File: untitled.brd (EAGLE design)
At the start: 59.4 x 57.8 mm, 25 parts

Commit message: made the traces look better
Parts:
- moved C2 0.32 mm to (56.2, 34.0)
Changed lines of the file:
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@@
 <element name="U$2" library="SparkFun" package="LCC36" value="HMC6343A" x="86.995" y="23.495"/>
 <element name="C1" library="rcl" package="C0603" value="" x="48.26" y="41.275" rot="R180"/>
-<element name="C2" library="rcl" package="C0603" value="" x="56.515" y="33.9725" rot="R180"/>
+<element name="C2" library="rcl" package="C0603" value="" x="56.1975" y="33.9725" rot="R180"/>
 <element name="C3" library="rcl" package="C0603" value="" x="53.6575" y="51.1175" rot="R90"/>
 <element name="C4" library="SparkFun" package="0603" value="" x="79.6925" y="25.0825" rot="R90"/>
@@
 <wire x1="66.04" y1="36.83" x2="66.04" y2="24.765" width="0.3048" layer="1"/>
 <wire x1="66.04" y1="24.765" x2="68.58" y2="24.765" width="0.3048" layer="1"/>
-<wire x1="57.4" y1="38.5313" x2="58.1025" y2="36.83" width="0.254" layer="1"/>
+<wire x1="57.4" y1="38.5313" x2="57.4" y2="37.5325" width="0.3048" layer="1"/>
+<wire x1="57.4" y1="37.5325" x2="58.1025" y2="36.83" width="0.3048" layer="1"/>
 </signal>
 <signal name="N$6">
@@
 <wire x1="70.8025" y1="24.13" x2="70.485" y2="27.305" width="0.3048" layer="1"/>
 <wire x1="70.485" y1="27.305" x2="68.58" y2="27.305" width="0.3048" layer="1"/>
-<wire x1="56.1" y1="38.5313" x2="56.8325" y2="35.8775" width="0.3048" layer="1"/>
-<wire x1="56.8325" y1="35.8775" x2="57.15" y2="35.56" width="0.3048" layer="1"/>
 <wire x1="57.15" y1="35.56" x2="59.055" y2="35.56" width="0.3048" layer="1"/>
+<wire x1="56.1" y1="38.5313" x2="56.1" y2="37.245" width="0.3048" layer="1"/>
+<wire x1="56.1" y1="37.245" x2="57.15" y2="35.56" width="0.3048" layer="1"/>
 </signal>
 <signal name="N$8">
@@
 <wire x1="66.9925" y1="26.035" x2="66.9925" y2="29.845" width="0.3048" layer="1"/>
 <wire x1="66.9925" y1="29.845" x2="68.58" y2="29.845" width="0.3048" layer="1"/>
-<wire x1="56.75" y1="38.5313" x2="56.75" y2="38.1825" width="0.3048" layer="1"/>
-<wire x1="56.75" y1="38.1825" x2="57.4675" y2="36.195" width="0.3048" layer="1"/>
+<wire x1="56.75" y1="38.5313" x2="56.75" y2="37.5475" width="0.3048" layer="1"/>
+<wire x1="56.75" y1="37.5475" x2="57.4675" y2="36.195" width="0.3048" layer="1"/>
 </signal>
 <signal name="SCL">
@@
 <vertex x="33.655" y="10.16"/>
 </polygon>
-<wire x1="54.8" y1="38.5313" x2="55.1175" y2="35.6875" width="0.4064" layer="1"/>
-<wire x1="55.245" y1="35.2425" x2="55.46" y2="34.925" width="0.4064" layer="1"/>
-<wire x1="55.46" y1="34.925" x2="55.665" y2="33.9725" width="0.4064" layer="1"/>
+<wire x1="55.1425" y1="34.925" x2="55.3475" y2="33.9725" width="0.4064" layer="1"/>
 <wire x1="54.8" y1="47.1313" x2="54.8" y2="52.07" width="0.4064" layer="1"/>
 <wire x1="54.8" y1="52.07" x2="54.4825" y2="53.4675" width="0.4064" layer="1"/>
@@
 <via x="48.26" y="42.8625" extent="1-16" drill="0.6"/>
 <via x="54.4825" y="53.4675" extent="1-16" drill="0.6"/>
-<via x="55.1175" y="35.6875" extent="1-16" drill="0.6"/>
+<via x="55.1175" y="35.37" extent="1-16" drill="0.6"/>
 <wire x1="59.1" y1="42.1813" x2="60.3712" y2="42.1813" width="0.4064" layer="1"/>
 <wire x1="60.3712" y1="42.1813" x2="60.6425" y2="41.5925" width="0.4064" layer="1"/>
 <via x="60.6425" y="41.5925" extent="1-16" drill="0.6"/>
-<wire x1="55.245" y1="35.2425" x2="55.1175" y2="35.6875" width="0.4064" layer="1"/>
 <wire x1="89.395" y1="27.895" x2="89.395" y2="25.54" width="0.3048" layer="1"/>
 <wire x1="89.395" y1="25.54" x2="89.84" y2="25.095" width="0.3048" layer="1"/>
@@
 <wire x1="42.545" y1="41.91" x2="47.625" y2="41.91" width="0.4064" layer="1"/>
 <wire x1="42.6025" y1="41.8525" x2="42.545" y2="41.91" width="0.4064" layer="1" curve="90"/>
+<wire x1="54.8" y1="38.5313" x2="54.8" y2="36.005" width="0.3048" layer="1"/>
+<wire x1="54.8" y1="36.005" x2="55.1175" y2="35.37" width="0.3048" layer="1"/>
+<wire x1="55.1425" y1="34.925" x2="55.1175" y2="34.95" width="0.3048" layer="1" curve="-90"/>
+<wire x1="55.1175" y1="34.95" x2="55.1175" y2="35.37" width="0.3048" layer="1"/>
+<wire x1="81.915" y1="60.325" x2="89.535" y2="60.325" width="0" layer="19" extent="1-1"/>
+<wire x1="81.915" y1="62.865" x2="81.915" y2="60.325" width="0" layer="19" extent="1-1"/>
+<wire x1="81.915" y1="57.785" x2="81.915" y2="60.325" width="0" layer="19" extent="1-1"/>
+<wire x1="81.915" y1="55.245" x2="81.915" y2="57.785" width="0" layer="19" extent="1-1"/>
+<wire x1="74.05" y1="43.755" x2="81.915" y2="55.245" width="0" layer="19" extent="1-1"/>
+<wire x1="80.3275" y1="30.7975" x2="75.2475" y2="36.195" width="0" layer="19" extent="1-1"/>
+<wire x1="60.6425" y1="41.5925" x2="68.58" y2="40.3225" width="0" layer="19" extent="1-1"/>
+<wire x1="54.8" y1="38.5313" x2="59.1" y2="42.1813" width="0" layer="19" extent="1-1"/>
+<wire x1="50.5" y1="42.8313" x2="54.8" y2="38.5313" width="0" layer="19" extent="1-1"/>
+<wire x1="54.8" y1="47.1313" x2="50.5" y2="43.4813" width="0" layer="19" extent="1-1"/>
+<wire x1="60.325" y1="59.69" x2="54.4825" y2="53.4675" width="0" layer="19" extent="1-1"/>
+<wire x1="57.785" y1="64.77" x2="60.325" y2="59.69" width="0" layer="19" extent="1-1"/>
+<wire x1="60.96" y1="24.765" x2="55.3475" y2="33.9725" width="0" layer="19" extent="1-1"/>
+<wire x1="70.77" y1="13.51" x2="75.2475" y2="27.6225" width="0" layer="19" extent="1-1"/>
+<wire x1="40.64" y1="66.04" x2="57.785" y2="64.77" width="0" layer="19" extent="1-1"/>
+<wire x1="36.83" y1="62.96" x2="40.64" y2="66.04" width="0" layer="19" extent="1-1"/>
 </signal>
 <signal name="+5V">
@@
 <wire x1="48.895" y1="39.6875" x2="48.895" y2="41.06" width="0.4064" layer="1"/>
 <wire x1="48.895" y1="41.06" x2="49.11" y2="41.275" width="0.4064" layer="1"/>
-<wire x1="57.365" y1="33.9725" x2="57.57" y2="33.235" width="0.4064" layer="1"/>
+<wire x1="57.0475" y1="33.9725" x2="57.57" y2="33.235" width="0.4064" layer="1"/>
 <wire x1="57.57" y1="33.235" x2="57.785" y2="32.7025" width="0.4064" layer="1"/>
 <via x="57.785" y="32.7025" extent="1-16" drill="0.6"/>
@@
 <wire x1="51.7525" y1="49.8475" x2="52.3875" y2="45.72" width="0.4064" layer="16"/>
 <wire x1="52.3875" y1="45.72" x2="53.6575" y2="44.45" width="0.4064" layer="16"/>
-<wire x1="55.7675" y1="36.5225" x2="57.365" y2="33.9725" width="0.4064" layer="1"/>
 <wire x1="60.96" y1="32.385" x2="60.96" y2="32.7025" width="0.4064" layer="16"/>
 <wire x1="60.96" y1="32.7025" x2="57.785" y2="32.7025" width="0.4064" layer="16"/>
@@
 <wire x1="35.2425" y1="40.64" x2="40.3225" y2="40.64" width="0.4064" layer="1"/>
 <wire x1="40.3225" y1="40.64" x2="40.3225" y2="21.9475" width="0.4064" layer="1"/>
-<wire x1="55.45" y1="38.5313" x2="55.7675" y2="36.5225" width="0.4064" layer="1"/>
+<wire x1="55.45" y1="38.5313" x2="55.45" y2="37.26" width="0.3048" layer="1"/>
+<wire x1="56.515" y1="34.505" x2="57.0475" y2="33.9725" width="0" layer="19" extent="1-16"/>
+<wire x1="55.45" y1="37.26" x2="56.8325" y2="34.925" width="0.3048" layer="1"/>
+<wire x1="56.8325" y1="34.925" x2="57.0475" y2="33.9725" width="0.3048" layer="1"/>
 </signal>
 </signals>

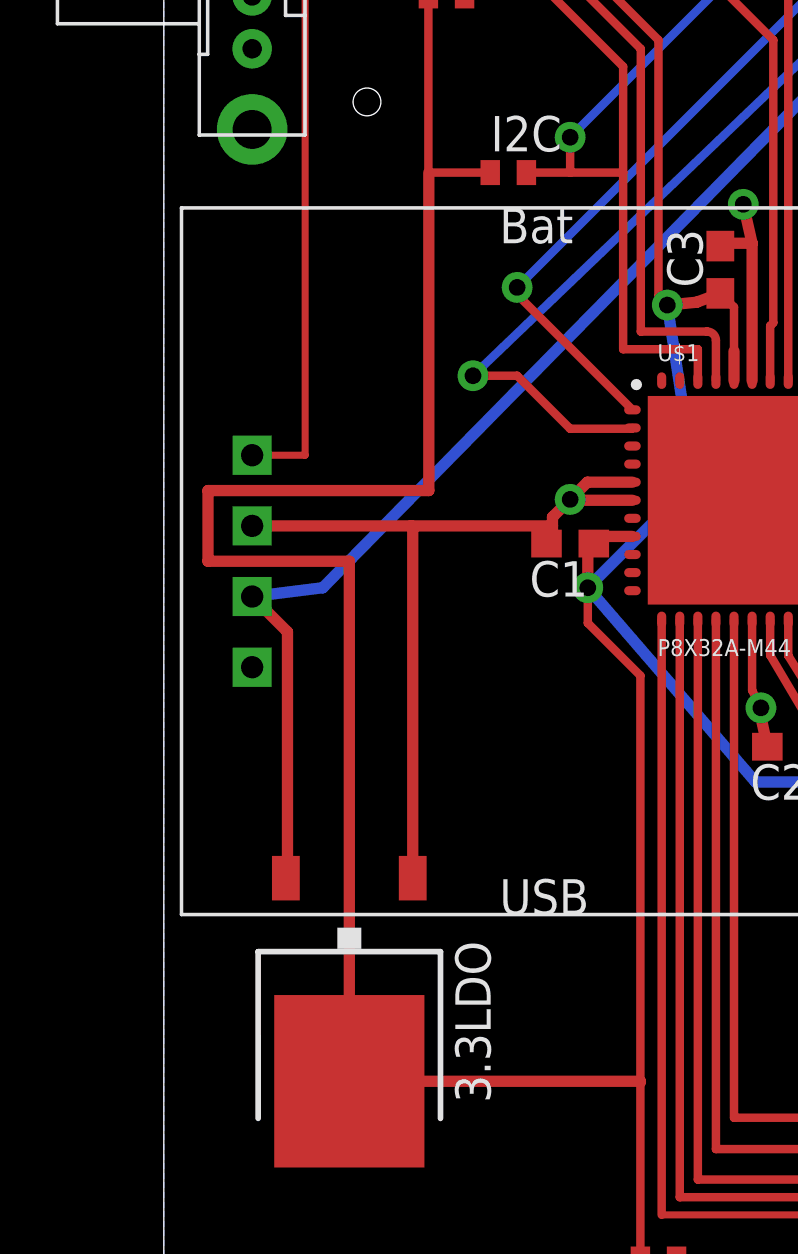
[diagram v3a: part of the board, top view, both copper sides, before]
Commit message: Redo crazy snaking +3V3 trace.
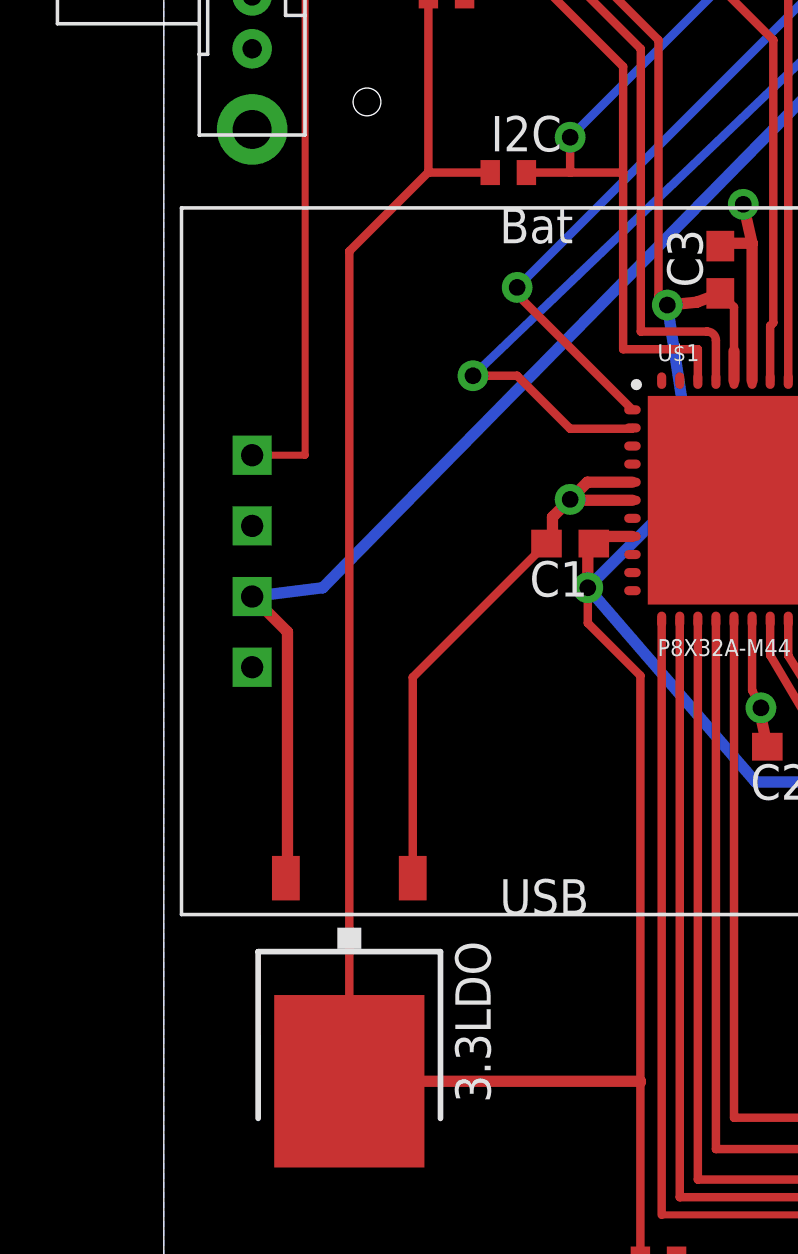
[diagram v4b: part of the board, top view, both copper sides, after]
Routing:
- net +3V3: track 302.4 -> 290.6 mm
- net GND: track 91.5 -> 82.1 mm
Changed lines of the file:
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@@
 <wire x1="50.5" y1="42.8313" x2="48.2288" y2="42.8313" width="0.4064" layer="1"/>
 <wire x1="48.2288" y1="42.8313" x2="47.625" y2="42.2275" width="0.4064" layer="1"/>
-<wire x1="47.625" y1="42.2275" x2="47.625" y2="41.91" width="0.4064" layer="1"/>
-<wire x1="47.625" y1="41.91" x2="47.625" y2="41.49" width="0.4064" layer="1"/>
+<wire x1="47.625" y1="42.2275" x2="47.625" y2="41.49" width="0.4064" layer="1"/>
 <wire x1="47.625" y1="41.49" x2="47.41" y2="41.275" width="0.4064" layer="1"/>
 <wire x1="50.5" y1="43.4813" x2="48.8788" y2="43.4813" width="0.4064" layer="1"/>
@@
 <wire x1="53.6575" y1="52.07" x2="54.8" y2="52.07" width="0.4064" layer="1"/>
 <contactref element="3.3LDO" pad="1"/>
-<wire x1="42.6025" y1="29.2475" x2="42.6025" y2="41.8525" width="0.4064" layer="1"/>
-<wire x1="36.83" y1="41.91" x2="42.545" y2="41.91" width="0.4064" layer="1"/>
-<wire x1="42.545" y1="41.91" x2="47.625" y2="41.91" width="0.4064" layer="1"/>
-<wire x1="42.6025" y1="41.8525" x2="42.545" y2="41.91" width="0.4064" layer="1" curve="90"/>
 <wire x1="54.8" y1="38.5313" x2="54.8" y2="36.005" width="0.3048" layer="1"/>
 <wire x1="54.8" y1="36.005" x2="55.1175" y2="35.37" width="0.3048" layer="1"/>
 <wire x1="55.1425" y1="34.925" x2="55.1175" y2="34.95" width="0.3048" layer="1" curve="-90"/>
 <wire x1="55.1175" y1="34.95" x2="55.1175" y2="35.37" width="0.3048" layer="1"/>
+<wire x1="42.6025" y1="29.2475" x2="42.6025" y2="36.4675" width="0.3048" layer="1"/>
+<wire x1="42.6025" y1="36.4675" x2="47.41" y2="41.275" width="0.3048" layer="1"/>
 <wire x1="81.915" y1="60.325" x2="89.535" y2="60.325" width="0" layer="19" extent="1-1"/>
 <wire x1="81.915" y1="62.865" x2="81.915" y2="60.325" width="0" layer="19" extent="1-1"/>
@@
 <wire x1="50.5" y1="42.8313" x2="54.8" y2="38.5313" width="0" layer="19" extent="1-1"/>
 <wire x1="54.8" y1="47.1313" x2="50.5" y2="43.4813" width="0" layer="19" extent="1-1"/>
+<wire x1="36.83" y1="41.91" x2="42.6025" y2="36.4675" width="0" layer="19" extent="1-1"/>
 <wire x1="60.325" y1="59.69" x2="54.4825" y2="53.4675" width="0" layer="19" extent="1-1"/>
 <wire x1="57.785" y1="64.77" x2="60.325" y2="59.69" width="0" layer="19" extent="1-1"/>
@@
 <wire x1="51.435" y1="59.3725" x2="51.435" y2="50.165" width="0.3048" layer="1"/>
 <wire x1="51.435" y1="50.165" x2="51.7525" y2="49.8475" width="0.3048" layer="1"/>
-<wire x1="45.3875" y1="54.61" x2="43.18" y2="54.61" width="0.3048" layer="1"/>
-<wire x1="43.165" y1="60.96" x2="43.165" y2="54.625" width="0.3048" layer="1"/>
-<wire x1="43.165" y1="54.625" x2="43.18" y2="54.61" width="0.3048" layer="1"/>
 <wire x1="91.395" y1="21.895" x2="84.595" y2="21.895" width="0.3048" layer="1"/>
 <wire x1="84.595" y1="21.895" x2="84.595" y2="19.095" width="0.3048" layer="1"/>
@@
 <wire x1="40.3225" y1="21.9475" x2="50.785" y2="21.9475" width="0.4064" layer="1"/>
 <wire x1="50.785" y1="21.9475" x2="50.785" y2="21.9075" width="0.4064" layer="1"/>
-<wire x1="43.18" y1="54.61" x2="43.18" y2="43.18" width="0.4064" layer="1"/>
-<wire x1="43.18" y1="43.18" x2="35.2425" y2="43.18" width="0.4064" layer="1"/>
-<wire x1="35.2425" y1="43.18" x2="35.2425" y2="40.64" width="0.4064" layer="1"/>
-<wire x1="35.2425" y1="40.64" x2="40.3225" y2="40.64" width="0.4064" layer="1"/>
-<wire x1="40.3225" y1="40.64" x2="40.3225" y2="21.9475" width="0.4064" layer="1"/>
 <wire x1="55.45" y1="38.5313" x2="55.45" y2="37.26" width="0.3048" layer="1"/>
-<wire x1="56.515" y1="34.505" x2="57.0475" y2="33.9725" width="0" layer="19" extent="1-16"/>
 <wire x1="55.45" y1="37.26" x2="56.8325" y2="34.925" width="0.3048" layer="1"/>
 <wire x1="56.8325" y1="34.925" x2="57.0475" y2="33.9725" width="0.3048" layer="1"/>
+<wire x1="43.18" y1="54.61" x2="45.3875" y2="54.61" width="0.3048" layer="1"/>
+<wire x1="43.165" y1="60.96" x2="43.165" y2="54.625" width="0.3048" layer="1"/>
+<wire x1="43.165" y1="54.625" x2="43.18" y2="54.61" width="0.3048" layer="1"/>
+<wire x1="40.3225" y1="21.9475" x2="40.3225" y2="51.7825" width="0.3048" layer="1"/>
+<wire x1="40.3225" y1="51.7825" x2="43.165" y2="54.625" width="0.3048" layer="1"/>
 </signal>
 </signals>
